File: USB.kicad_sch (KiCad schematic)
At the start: 16 parts, among them J6 USB_C_Receptacle_USB2.0_16P, U13 TPD4EUSB30, U6 CP2102N-A02-GQFN24R

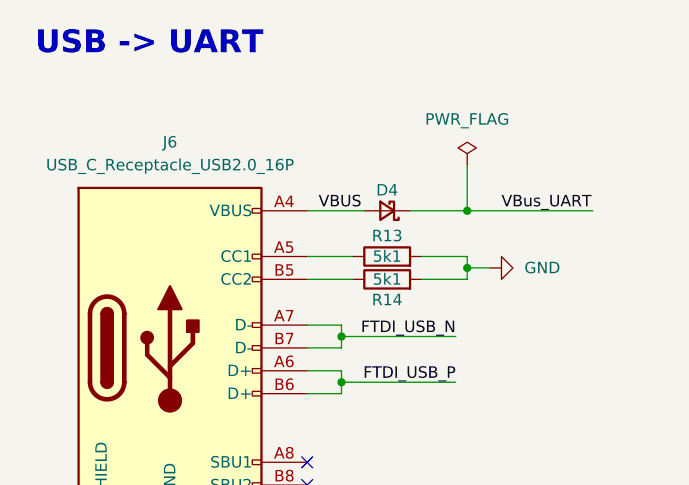
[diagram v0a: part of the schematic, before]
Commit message: wip: add button
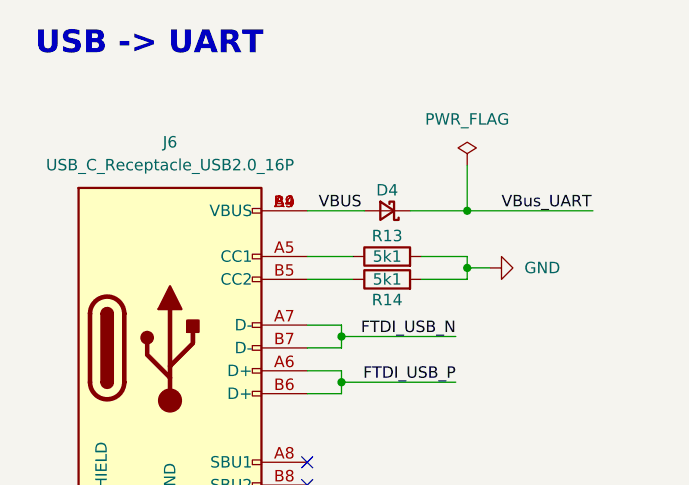
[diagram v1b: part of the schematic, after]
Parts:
- J6: footprint Hardware Components:USB_C_Receptacle_HRO_TYPE-C-31-M-12 -> Hardware Components:USB_C_Receptacle_XUNPU_TYPEC-305-ACP16H458; symbol Hardware Components:USB_C_Receptacle_HRO_TYPE-C-31-M-12 -> Hardware Components:USB_C_Receptacle_XUNPU_TYPEC-305-ACP16H458; JLCPCB Part # C165948 -> C5454943; MPN TYPE-C-31-M-12 -> TYPEC-305-ACP16H458; Manufacturer Korean Hroparts Elec -> XUNPU
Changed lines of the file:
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@@
 	)
 	(symbol
-		(lib_id "Hardware Components:USB_C_Receptacle_HRO_TYPE-C-31-M-12")
+		(lib_id "Hardware Components:USB_C_Receptacle_XUNPU_TYPEC-305-ACP16H458")
 		(at 36.83 54.61 0)
 		(unit 1)
@@
 			)
 		)
-		(property "Footprint" "Hardware Components:USB_C_Receptacle_HRO_TYPE-C-31-M-12"
-			(at 40.64 54.61 0)
+		(property "Footprint" "Hardware Components:USB_C_Receptacle_XUNPU_TYPEC-305-ACP16H458"
+			(at 36.576 83.82 0)
 			(effects
 				(font
@@
 			)
 		)
-		(property "Datasheet" "https://www.usb.org/sites/default/files/documents/usb_type-c.zip"
-			(at 40.64 54.61 0)
+		(property "Datasheet" "https://jlcpcb.com/api/file/downloadByFileSystemAccessId/8590904324467863552"
+			(at 36.83 80.772 0)
 			(effects
 				(font
@@
 			)
 		)
-		(property "Description" "USB 2.0-only 16P Type-C Receptacle connector"
+		(property "Description" "-55℃~+85℃ 1 16P 5A Female Side View Mount Type-C USB 3.1 SMD USB Connectors ROHS"
+			(at 37.846 87.884 0)
+			(effects
+				(font
+					(size 1.27 1.27)
+				)
+				(hide yes)
+			)
+		)
+		(property "MPN" "TYPEC-305-ACP16H458"
+			(at 37.084 90.932 0)
+			(effects
+				(font
+					(size 1.27 1.27)
+				)
+				(hide yes)
+			)
+		)
+		(property "Manufacturer" "XUNPU"
 			(at 36.83 54.61 0)
 			(effects
@@
 			)
 		)
-		(property "MPN" "TYPE-C-31-M-12"
-			(at 36.83 54.61 0)
+		(property "JLCPCB Part #" "C5454943"
+			(at 35.56 91.948 0)
 			(effects
 				(font
-					(size 1.27 1.27)
-				)
-				(hide yes)
-			)
-		)
-		(property "Manufacturer" "Korean Hroparts Elec"
-			(at 36.83 54.61 0)
-			(effects
-				(font
-					(size 1.27 1.27)
-				)
-				(hide yes)
-			)
-		)
-		(property "JLCPCB Part #" "C165948"
-			(at 36.83 54.61 0)
-			(effects
-				(font
